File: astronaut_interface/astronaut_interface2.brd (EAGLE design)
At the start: 61.9 x 53.3 mm, 17 parts, among them IC1 PCF8591T, J1 UI, J2 Display, P1 JT9S-19, U1 TACT-12MM, U2 TACT-12MM, U3 TACT-12MM, U4 TACT-12MM

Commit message: verified, ready to production
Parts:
- moved JP1 2.54 mm to (12.7, 6.35)
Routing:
- net +5V: track 162.9 -> 160.0 mm
- net GND: track 109.7 -> 112.3 mm
- net A0: track 11.7 -> 12.4 mm
- added copper zone on layer 1, net GND
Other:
- board text added: "Astronaut UI IGLUNA Mar'19 by M. Kazaniecki"
- board text removed: "Astronaut UI IGLUNA Feb'19 by MK"
- board text removed: "prostokąt to moduł wyświetlacza 4x20 (całe PCB)"

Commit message: final, after another review
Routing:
- net I2C_SCL: track 47.7 -> 53.9 mm

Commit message: really final projects, added gerber files
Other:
- board text added: "+"
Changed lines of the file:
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@@
 <layer number="19" name="Unrouted" color="6" fill="1" visible="yes" active="yes"/>
 <layer number="20" name="Dimension" color="15" fill="1" visible="yes" active="yes"/>
-<layer number="21" name="tPlace" color="7" fill="1" visible="yes" active="yes"/>
-<layer number="22" name="bPlace" color="7" fill="1" visible="yes" active="yes"/>
+<layer number="21" name="tPlace" color="7" fill="1" visible="no" active="yes"/>
+<layer number="22" name="bPlace" color="7" fill="1" visible="no" active="yes"/>
 <layer number="23" name="tOrigins" color="15" fill="1" visible="yes" active="yes"/>
 <layer number="24" name="bOrigins" color="15" fill="1" visible="yes" active="yes"/>
@@
 <layer number="27" name="tValues" color="7" fill="1" visible="yes" active="yes"/>
 <layer number="28" name="bValues" color="7" fill="1" visible="yes" active="yes"/>
-<layer number="29" name="tStop" color="7" fill="3" visible="no" active="yes"/>
-<layer number="30" name="bStop" color="7" fill="6" visible="no" active="yes"/>
-<layer number="31" name="tCream" color="7" fill="4" visible="no" active="yes"/>
-<layer number="32" name="bCream" color="7" fill="5" visible="no" active="yes"/>
-<layer number="33" name="tFinish" color="6" fill="3" visible="no" active="yes"/>
-<layer number="34" name="bFinish" color="6" fill="6" visible="no" active="yes"/>
-<layer number="35" name="tGlue" color="7" fill="4" visible="no" active="yes"/>
-<layer number="36" name="bGlue" color="7" fill="5" visible="no" active="yes"/>
-<layer number="37" name="tTest" color="7" fill="1" visible="no" active="yes"/>
-<layer number="38" name="bTest" color="7" fill="1" visible="no" active="yes"/>
+<layer number="29" name="tStop" color="7" fill="3" visible="yes" active="yes"/>
+<layer number="30" name="bStop" color="7" fill="6" visible="yes" active="yes"/>
+<layer number="31" name="tCream" color="7" fill="4" visible="yes" active="yes"/>
+<layer number="32" name="bCream" color="7" fill="5" visible="yes" active="yes"/>
+<layer number="33" name="tFinish" color="6" fill="3" visible="yes" active="yes"/>
+<layer number="34" name="bFinish" color="6" fill="6" visible="yes" active="yes"/>
+<layer number="35" name="tGlue" color="7" fill="4" visible="yes" active="yes"/>
+<layer number="36" name="bGlue" color="7" fill="5" visible="yes" active="yes"/>
+<layer number="37" name="tTest" color="7" fill="1" visible="yes" active="yes"/>
+<layer number="38" name="bTest" color="7" fill="1" visible="yes" active="yes"/>
 <layer number="39" name="tKeepout" color="4" fill="11" visible="yes" active="yes"/>
 <layer number="40" name="bKeepout" color="1" fill="11" visible="yes" active="yes"/>
@@
 <layer number="42" name="bRestrict" color="1" fill="10" visible="yes" active="yes"/>
 <layer number="43" name="vRestrict" color="2" fill="10" visible="yes" active="yes"/>
-<layer number="44" name="Drills" color="7" fill="1" visible="no" active="yes"/>
+<layer number="44" name="Drills" color="7" fill="1" visible="yes" active="yes"/>
 <layer number="45" name="Holes" color="7" fill="1" visible="yes" active="yes"/>
-<layer number="46" name="Milling" color="3" fill="1" visible="no" active="yes"/>
-<layer number="47" name="Measures" color="7" fill="1" visible="no" active="yes"/>
+<layer number="46" name="Milling" color="3" fill="1" visible="yes" active="yes"/>
+<layer number="47" name="Measures" color="7" fill="1" visible="yes" active="yes"/>
 <layer number="48" name="Document" color="7" fill="1" visible="yes" active="yes"/>
 <layer number="49" name="Reference" color="7" fill="1" visible="yes" active="yes"/>
@@
 <layer number="112" name="tSilk" color="7" fill="1" visible="yes" active="yes"/>
 <layer number="113" name="IDFDebug" color="4" fill="1" visible="yes" active="yes"/>
-<layer number="114" name="Badge_Outline" color="7" fill="1" visible="no" active="yes"/>
-<layer number="115" name="ReferenceISLANDS" color="7" fill="1" visible="no" active="yes"/>
+<layer number="114" name="Badge_Outline" color="7" fill="1" visible="yes" active="yes"/>
+<layer number="115" name="ReferenceISLANDS" color="7" fill="1" visible="yes" active="yes"/>
 <layer number="116" name="Patch_BOT" color="9" fill="4" visible="yes" active="yes"/>
-<layer number="118" name="Rect_Pads" color="7" fill="1" visible="no" active="yes"/>
+<layer number="118" name="Rect_Pads" color="7" fill="1" visible="yes" active="yes"/>
 <layer number="121" name="_tsilk" color="7" fill="1" visible="yes" active="yes"/>
 <layer number="122" name="_bsilk" color="7" fill="1" visible="yes" active="yes"/>
@@
 <text x="14.605" y="4.445" size="1.27" layer="25" font="vector" ratio="15" rot="R270">GND</text>
 <text x="12.065" y="4.445" size="1.27" layer="25" font="vector" ratio="15" rot="R270">A0</text>
+<text x="12.065" y="31.75" size="1.27" layer="25" font="vector" ratio="15">+</text>
 </plain>
 <attributes>
@@
 </class>
 </classes>
-<designrules name="default *">
+<designrules name="jlcpcb_rules">
 <description language="de">&lt;b&gt;EAGLE Design Rules&lt;/b&gt;
 &lt;p&gt;
@@
 <param name="mtCopper" value="0.035mm 0.035mm 0.035mm 0.035mm 0.035mm 0.035mm 0.035mm 0.035mm 0.035mm 0.035mm 0.035mm 0.035mm 0.035mm 0.035mm 0.035mm 0.035mm"/>
 <param name="mtIsolate" value="1.5mm 0.15mm 0.2mm 0.15mm 0.2mm 0.15mm 0.2mm 0.15mm 0.2mm 0.15mm 0.2mm 0.15mm 0.2mm 0.15mm 0.2mm"/>
-<param name="mdWireWire" value="12mil"/>
-<param name="mdWirePad" value="12mil"/>
-<param name="mdWireVia" value="12mil"/>
-<param name="mdPadPad" value="10mil"/>
-<param name="mdPadVia" value="12mil"/>
-<param name="mdViaVia" value="12mil"/>
-<param name="mdSmdPad" value="10mil"/>
-<param name="mdSmdVia" value="10mil"/>
-<param name="mdSmdSmd" value="10mil"/>
-<param name="mdViaViaSameLayer" value="8mil"/>
+<param name="mdWireWire" value="5mil"/>
+<param name="mdWirePad" value="5mil"/>
+<param name="mdWireVia" value="5mil"/>
+<param name="mdPadPad" value="5mil"/>
+<param name="mdPadVia" value="5mil"/>
+<param name="mdViaVia" value="5mil"/>
+<param name="mdSmdPad" value="5mil"/>
+<param name="mdSmdVia" value="5mil"/>
+<param name="mdSmdSmd" value="5mil"/>
+<param name="mdViaViaSameLayer" value="6mil"/>
 <param name="mnLayersViaInSmd" value="2"/>
-<param name="mdCopperDimension" value="20mil"/>
+<param name="mdCopperDimension" value="0.2mm"/>
 <param name="mdDrill" value="12mil"/>
 <param name="mdSmdStop" value="0mil"/>
-<param name="msWidth" value="12mil"/>
-<param name="msDrill" value="24mil"/>
+<param name="msWidth" value="5mil"/>
+<param name="msDrill" value="0.2mm"/>
 <param name="msMicroVia" value="9.99mm"/>
 <param name="msBlindViaRatio" value="0.5"/>
@@
 <param name="rvMicroViaOuter" value="0.25"/>
 <param name="rvMicroViaInner" value="0.25"/>
-<param name="rlMinPadTop" value="10mil"/>
+<param name="rlMinPadTop" value="3mil"/>
 <param name="rlMaxPadTop" value="20mil"/>
 <param name="rlMinPadInner" value="10mil"/>
@@
 <param name="rlMinPadBottom" value="10mil"/>
 <param name="rlMaxPadBottom" value="20mil"/>
-<param name="rlMinViaOuter" value="8mil"/>
+<param name="rlMinViaOuter" value="3mil"/>
 <param name="rlMaxViaOuter" value="20mil"/>
 <param name="rlMinViaInner" value="8mil"/>
@@
 <element name="P1" library="jt9s-1p" package="JT9S-1P" value="JT9S-19" x="42.545" y="11.43" smashed="yes"/>
 <element name="R1" library="rcl" package="R0805" value="1k" x="34.29" y="44.45" smashed="yes" rot="MR270">
-<attribute name="NAME" x="34.29" y="48.26" size="1.016" layer="26" font="vector" ratio="15" rot="MR270"/>
+<attribute name="NAME" x="35.56" y="43.815" size="1.016" layer="26" font="vector" ratio="15" rot="MR90"/>
 </element>
 <element name="R2" library="rcl" package="R0805" value="1k" x="50.8" y="44.45" smashed="yes" rot="MR270">
-<attribute name="NAME" x="50.8" y="48.26" size="1.016" layer="26" font="vector" ratio="15" rot="MR270"/>
+<attribute name="NAME" x="52.07" y="43.815" size="1.016" layer="26" font="vector" ratio="15" rot="MR90"/>
 </element>
 <element name="R3" library="rcl" package="R0805" value="1k" x="48.895" y="30.48" smashed="yes" rot="MR90">
-<attribute name="NAME" x="49.53" y="34.29" size="1.016" layer="26" font="vector" ratio="15" rot="MR270"/>
+<attribute name="NAME" x="50.165" y="29.845" size="1.016" layer="26" font="vector" ratio="15" rot="MR90"/>
 </element>
 <element name="R4" library="rcl" package="R0805" value="1k" x="52.705" y="30.48" smashed="yes" rot="MR90">
-<attribute name="NAME" x="52.705" y="26.67" size="1.016" layer="26" font="vector" ratio="15" rot="MR90"/>
+<attribute name="NAME" x="53.975" y="29.845" size="1.016" layer="26" font="vector" ratio="15" rot="MR90"/>
 </element>
 <element name="R5" library="resistor" package="M0805" value="470" x="22.225" y="27.94" smashed="yes" rot="MR180">

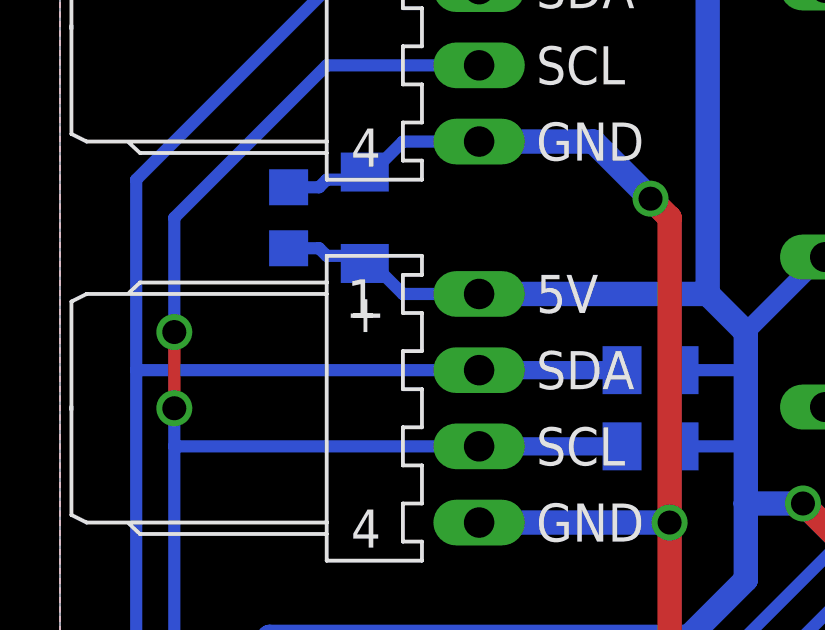
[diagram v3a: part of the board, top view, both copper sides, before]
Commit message: corrected gerbers, cleaned schematics, added documnetation
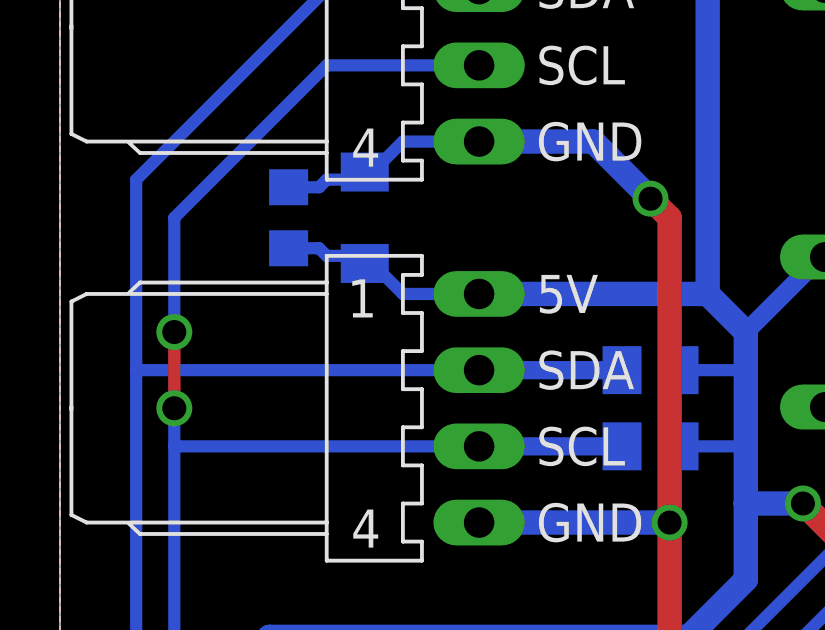
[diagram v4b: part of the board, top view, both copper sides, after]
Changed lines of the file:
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@@
 <text x="14.605" y="4.445" size="1.27" layer="25" font="vector" ratio="15" rot="R270">GND</text>
 <text x="12.065" y="4.445" size="1.27" layer="25" font="vector" ratio="15" rot="R270">A0</text>
-<text x="12.065" y="31.75" size="1.27" layer="25" font="vector" ratio="15">+</text>
+<text x="12.065" y="31.75" size="1.27" layer="26" font="vector" ratio="15">+</text>
 </plain>
 <attributes>
